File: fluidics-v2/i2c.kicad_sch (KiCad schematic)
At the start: 4 parts, among them U3 LTC4311CSC6-TRPBF

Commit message: V3: strip to minimal fluidics config, add 6th selector valve, fix lib paths
Reduce the V2 fluidics controller to a minimal build and extend the
selector-valve bank:

- Remove disc-pump driver (U1, M1); keep the syringe pump only
- Remove the solenoid-valve subsystem (MCZ33996 IC1 + D5-D20 + R6-R21
  + connector J5) -- 16 solenoids -> 0
- Remove all SPI pressure sensors (IC3-IC6 and their passives) -- 4 -> 0
- Reduce I2C flow sensors 4 -> 3 (drop connector J17)
- Add a 6th IDEX selector-valve channel (connectors J24/J25) on the
  shared isolated-I2C + 24V bus
- Remove the Wenzel-lab pressure-controller daughter board interface
  (J6, J7/ICSP, J8, JP3)
- Remove the manual-control block (switches S1-S4, push-button SW1,
  potentiometer VR1, TCA9539 U7, pull-ups, jumpers)
- Remove the 24V->12V converter (U5 + indicator D1/R2 + power-good R52);
  no remaining 12V load after the above

Net component count: 177 -> 86 footprints. DRC: 0 unconnected.

Tooling/portability fixes:
- Rewrite fp-lib-table and sym-lib-table: replace the original author's
  hardcoded absolute paths (/home/octopi-codex/...) with ${KIPRJMOD}-
  relative URIs so the libraries resolve on any machine
- Migrate the project to KiCad 10 format
- Add .gitignore for KiCad lock/autosave/cache and editor history files
- Add fluidics-v3-schematic.pdf (rendered schematic for review)

Co-Authored-By: Claude Opus 4.8 (1M context) <noreply@anthropic.com>
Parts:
- gave numbers to parts that had none: 1
- renumbered R2 to R39, R3 to R40, U3 to U8

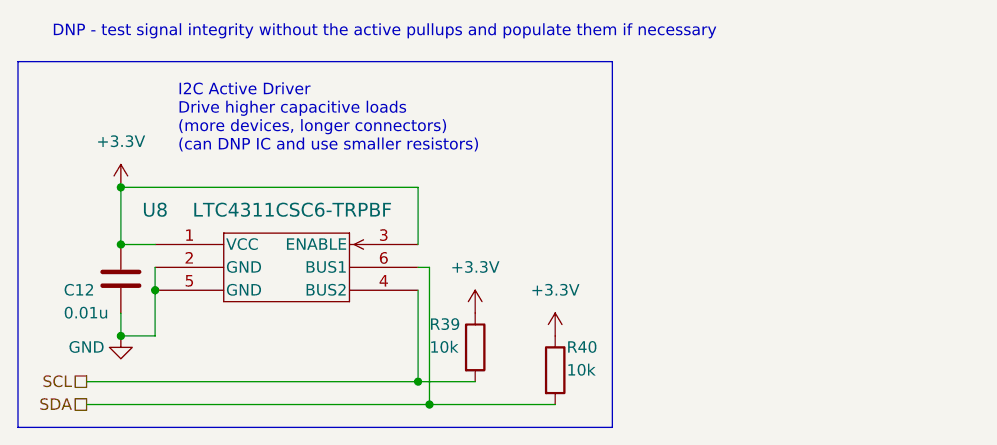
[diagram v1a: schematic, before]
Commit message: @ Wire solenoid driver + status LEDs + I2C cleanup; route + connect
- Solenoid driver (U1 TPL7407): IN1-7 <- Teensy GPIO_1-7 (back-layer fanout,
  vias off the SMD pads), COM->+24V, GND->plane, OUT1-7 -> J5 screw terminal
- Add 7 solenoid status LEDs (GPIO_1-7) + COM/+24V indicator LED (0402)
- Remove LTC4311 I2C accelerators (U9/U10) - misbehaved on lightly-loaded
  buses (single-valve failure); kept passive pull-ups. Restored SCL2/SDA2
  pull-ups (R41/R42)
- Back layer: full-board GND pour (clean rectangle outline)
- Connect U1 GND and R4 (+24V power-indicator LED) to their nets

DRC: unconnected down to 5, all intentional unused-pin no-connects
(GPIO_8/9 + vestigial SPI). No shorts; vias cleared out of Teensy SMD pads.

Co-Authored-By: Claude Opus 4.8 (1M context) <noreply@anthropic.com>
@
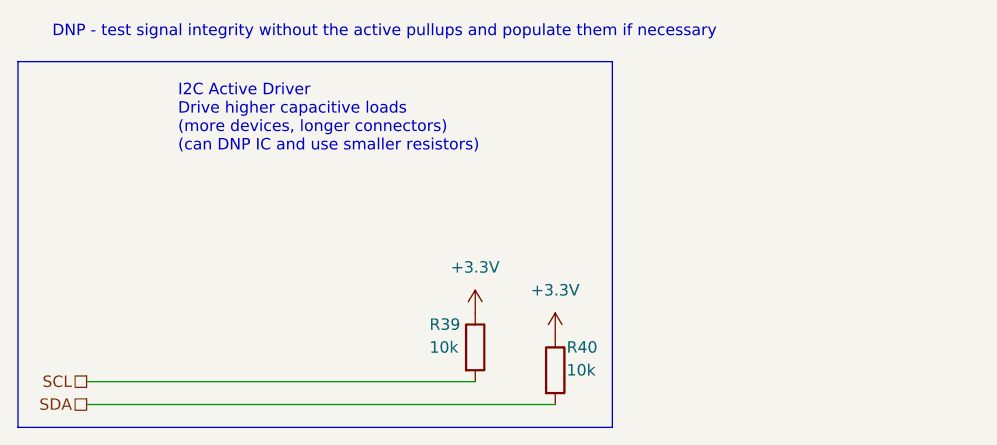
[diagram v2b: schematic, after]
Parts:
- removed C12: 0.01u, Capacitor_SMD:C_0603_1608Metric, symbol Device:C
- removed U8: LTC4311CSC6-TRPBF, SOT-6_SC_LIT, symbol LTC4311CSC6#TRPBF:LTC4311CSC6-TRPBF

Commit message: Place Cephla logo on F.SilkS (30%), add logo footprints; i2c sheet edit
- Placed bitmap2component logo (ref G***) on front silkscreen, scaled
  to 30% of original -> 12.40 x 4.88 mm; footprints 75 -> 76.
- Add logo source footprints: ImageCephlaCompanyPCB.kicad_mod (full)
  + _30pct (placed variant). Abandoned Attempt2/3 left untracked.
- i2c.kicad_sch: non-component edit (wiring/label), saved from GUI.

Co-Authored-By: Claude Opus 4.8 (1M context) <noreply@anthropic.com>
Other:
- note added: "I2C Pull-ups Drive higher capacitive loads (more devices, longer connectors) (can DNP IC and use smaller resistors)"
- note removed: "DNP - test signal integrity without the active pullups and populate them if necessary"
- note removed: "I2C Active Driver Drive higher capacitive loads (more devices, longer connectors) (can DNP IC and use smaller resistors)"
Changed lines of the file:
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@@
 		)
 	)
-	(text "DNP - test signal integrity without the active pullups and populate them if necessary"
-		(exclude_from_sim no)
-		(at 99.06 44.45 0)
-		(effects
-			(font
-				(size 1.27 1.27)
-			)
-			(justify left bottom)
-		)
-	)
-	(text "I2C Active Driver\nDrive higher capacitive loads\n(more devices, longer connectors)\n(can DNP IC and use smaller resistors)"
+	(text "I2C Pull-ups\nDrive higher capacitive loads\n(more devices, longer connectors)\n(can DNP IC and use smaller resistors)"
 		(exclude_from_sim no)
 		(at 113.03 57.15 0)
